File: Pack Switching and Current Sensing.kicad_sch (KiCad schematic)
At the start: 26 parts, among them Q29 CSD19531Q5A, Q30 CSD19531Q5A, Q31 ZXMP10A13F, Q32 CSD19531Q5A, Q33 CSD19531Q5A

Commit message: worked on MCU
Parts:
- renumbered C60 to C24, C62 to C25, C63 to C26, C64 to C27, D79 to D27, D80 to D28, E2 to E1, FB5 to FB1, FB6 to FB2, FB7 to FB3, FB8 to FB4, NT2 to NT1, Q29 to Q11, Q30 to Q12, Q31 to Q13, Q32 to Q14, Q33 to Q15, R153 to R62, R154 to R63, R157 to R64, R158 to R65, R159 to R66, R160 to R67, R163 to R68, R265 to R69, R165 to R70
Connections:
- net SCREW_BATT+ renamed BATT+

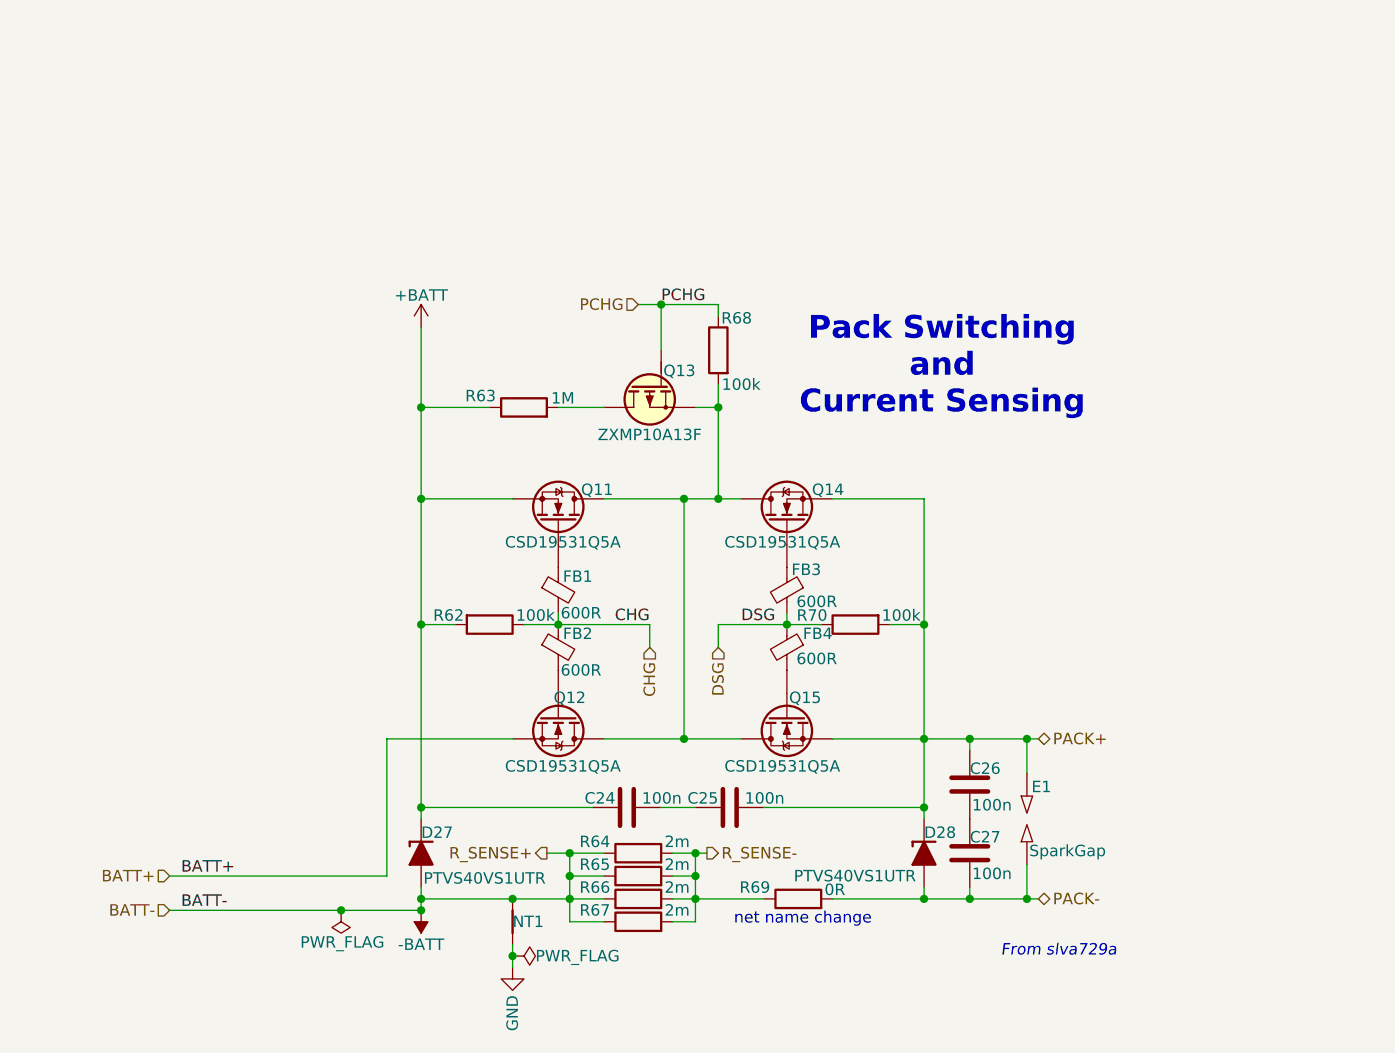
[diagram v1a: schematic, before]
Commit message: Added Fuel/Gas Guage
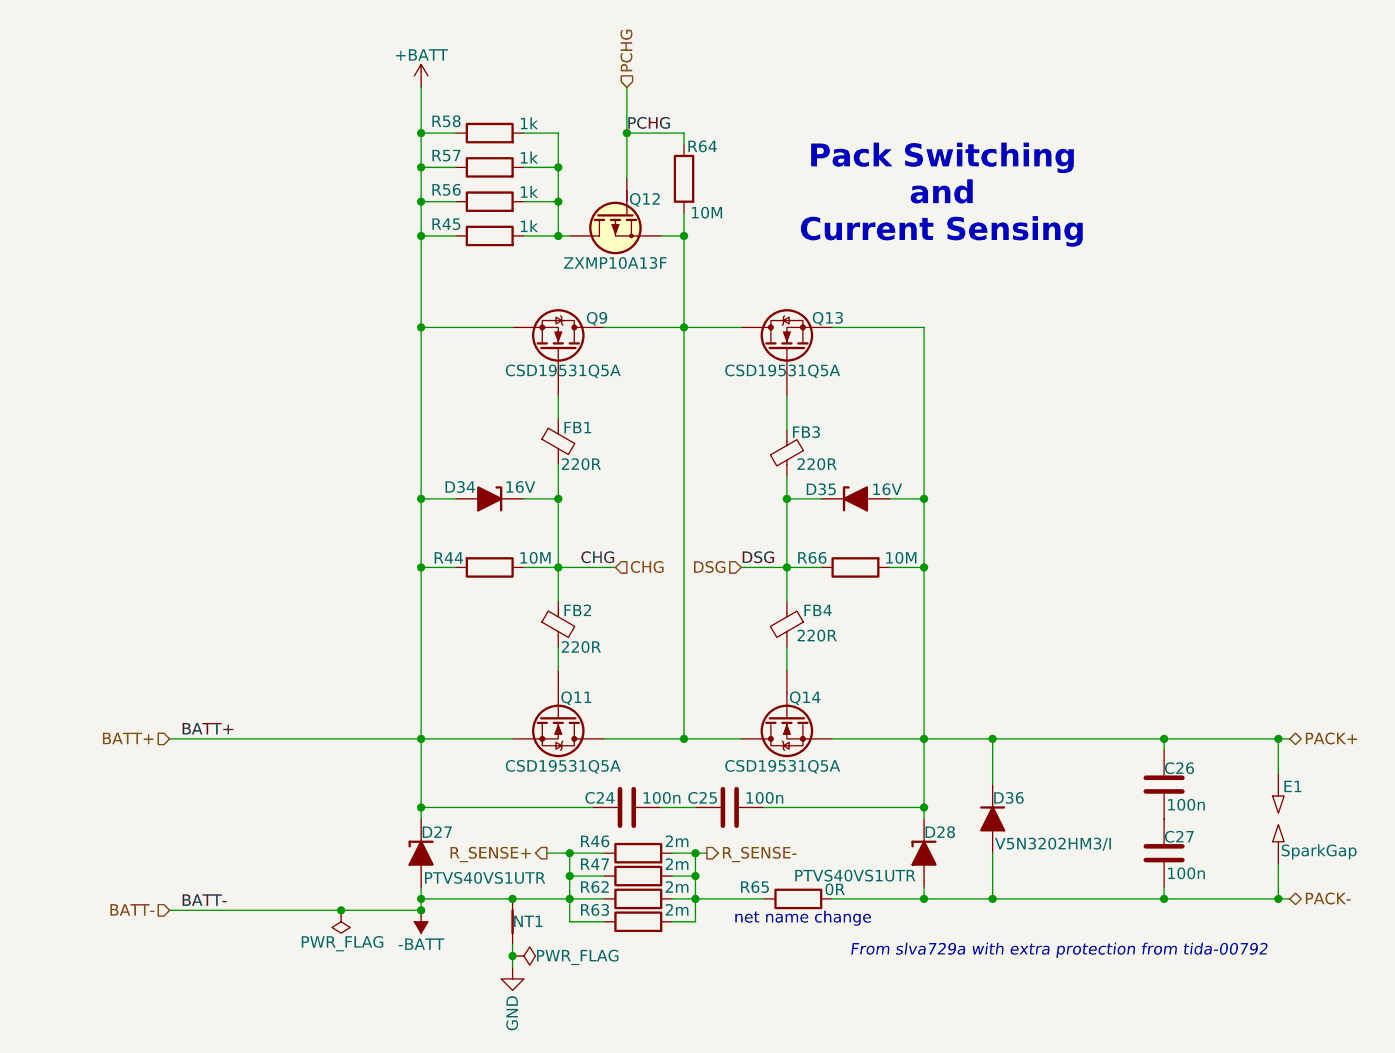
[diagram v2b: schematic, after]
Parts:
- added D34, D35: 16V, symbol Device:D_Zener_Filled
- added D36: V5N3202HM3/I, symbol Device:D_Filled
- added R56, R57, R58: 1k, symbol Device:R
- FB1, FB2, FB3, FB4: value 600R -> 220R
- R44: renamed from R62; value 100k -> 10M
- R45: renamed from R63; value 1M -> 1k
- R64: renamed from R68; value 100k -> 10M
- R66: renamed from R70; value 100k -> 10M
- renumbered Q12 to Q11, Q13 to Q12, Q14 to Q13, Q15 to Q14, Q11 to Q9, R64 to R46, R65 to R47, R66 to R62, R67 to R63, R69 to R65
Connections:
- net BATT+ is gone; now on net +BATT: Q11.1 (S), Q11.2 (S), Q11.3 (S)
- net +BATT: now also D34.2 (A), R56.1, R57.1, R58.1
- net CHG: now also D34.1 (K)
- net DSG: now also D35.1 (K)
- net PACK+: now also D35.2 (A), D36.1 (K)
- net PACK-: now also D36.2 (A)
- net at Q12.3 (D), R45.2: now also R56.2, R57.2, R58.2
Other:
- note added: "From slva729a with extra protection from tida-00792"
- note removed: "From slva729a"
- moved on the sheet: C26, C27, E1, FB1, FB2, FB3, FB4, Q12, Q13, Q9, R44, R45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

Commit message: ready to start first pass review on bms
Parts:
- removed R65: 0R, symbol Device:R
- D24: renamed from D34; value 16V -> 18V
- D25: renamed from D35; value 16V -> 18V
- renumbered C24 to C19, C25 to C20, C26 to C21, C27 to C22, D27 to D23, D28 to D26, D36 to D27, Q11 to Q10, Q12 to Q11, Q13 to Q12, Q14 to Q13, R58 to R44, R57 to R45, R56 to R46, R45 to R47, R44 to R48, R46 to R49, R47 to R50, R62 to R51, R63 to R52, R64 to R53, R66 to R54
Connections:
- net R_SENSE- is gone; now on net PACK-: R49.2, R50.2, R51.2, R52.2
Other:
- note removed: "net name change"

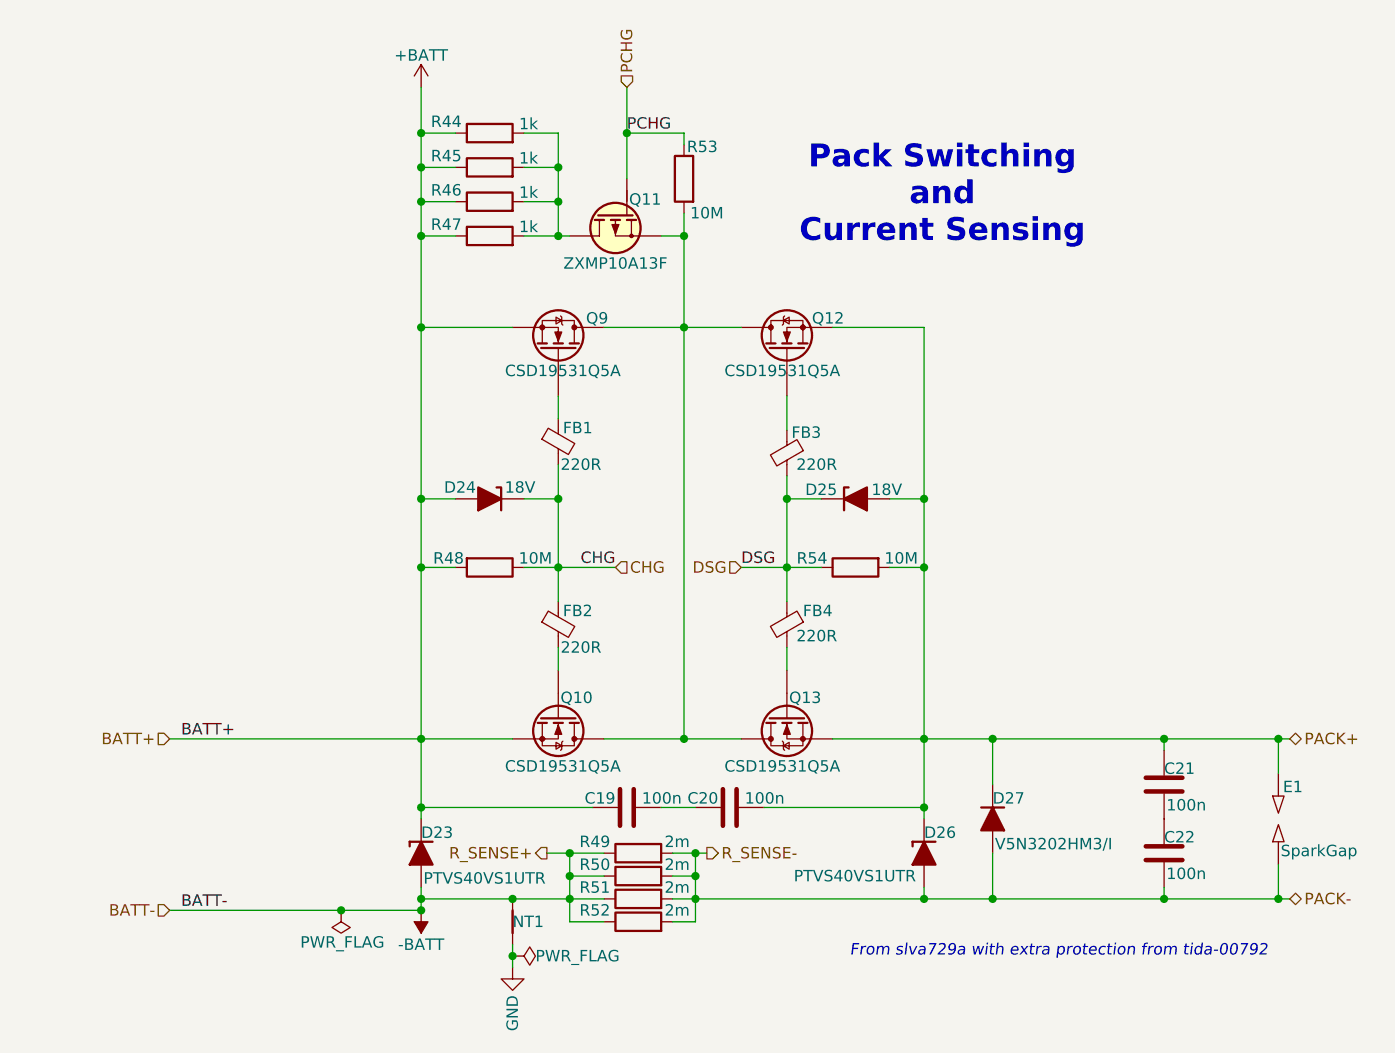
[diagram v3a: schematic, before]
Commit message: I still need to add the 6V line and test points
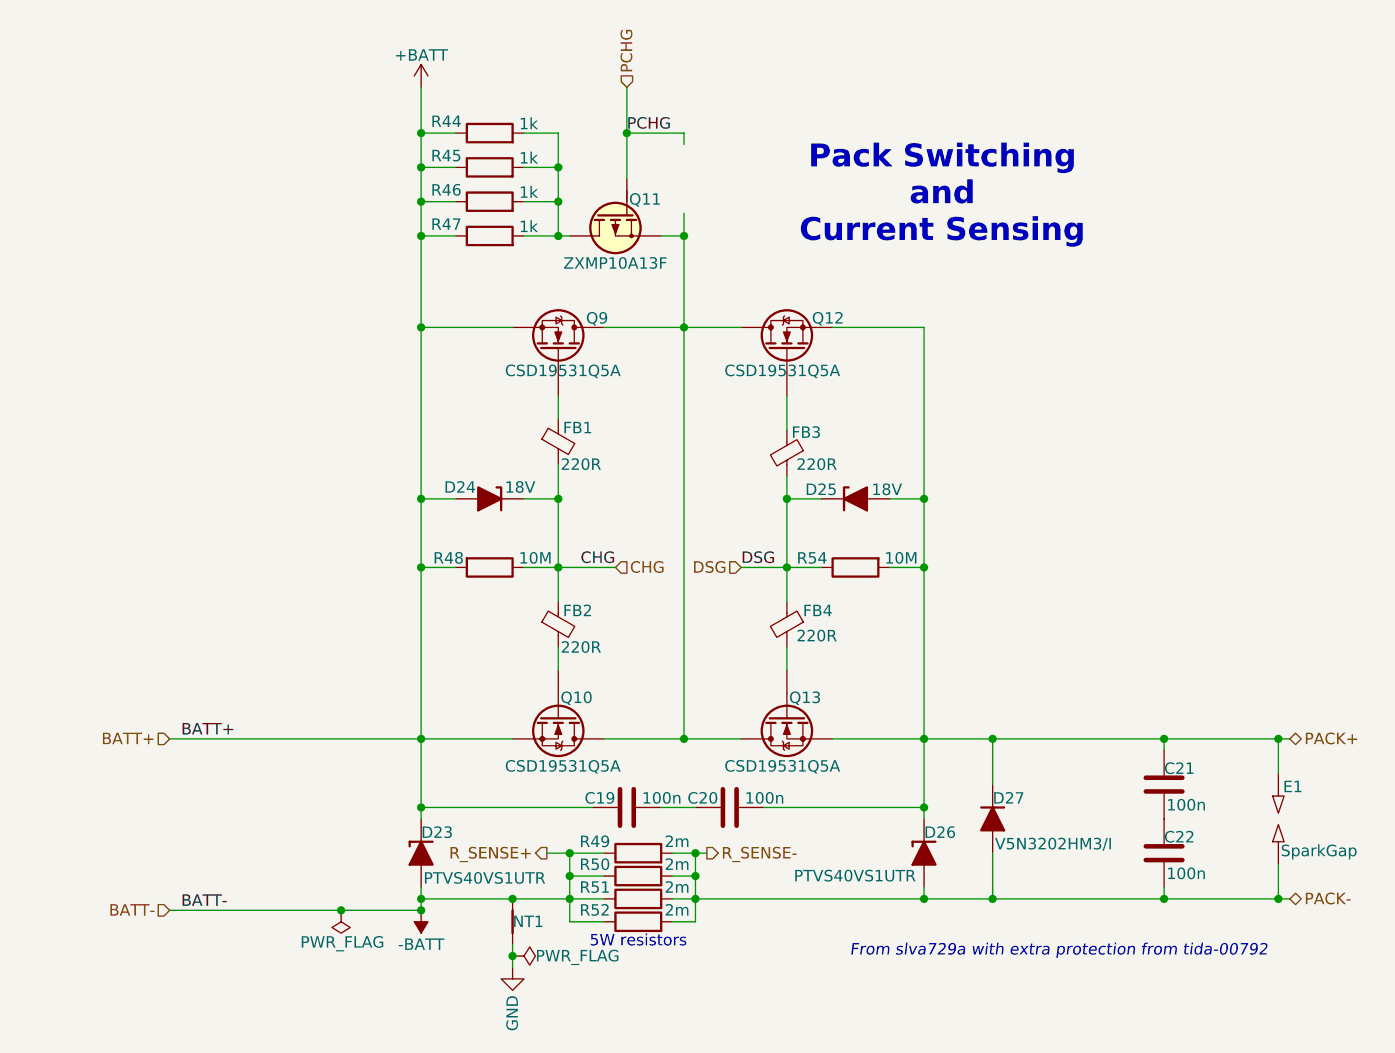
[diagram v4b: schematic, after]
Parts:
- removed R53: 10M, symbol Device:R
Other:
- note added: "5W resistors"
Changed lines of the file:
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@@
 		)
 	)
+	(text "5W resistors"
+		(exclude_from_sim no)
+		(at 140.97 125.476 0)
+		(effects
+			(font
+				(size 1.27 1.27)
+			)
+		)
+	)
 	(junction
 		(at 132.08 43.18)
@@
 					(unit 1)
 				)
-			)
-		)
-	)
-	(symbol
-		(lib_id "Device:R")
-		(at 146.05 40.64 0)
-		(mirror y)
-		(unit 1)
-		(exclude_from_sim no)
-		(in_bom yes)
-		(on_board yes)
-		(dnp no)
-		(property "Reference" "R53"
-			(at 148.082 37.084 0)
-			(effects
-				(font
-					(size 1.27 1.27)
-				)
-			)
-		)
-		(property "Value" "10M"
-			(at 148.59 44.45 0)
-			(effects
-				(font
-					(size 1.27 1.27)
-				)
-			)
-		)
-		(property "Footprint" ""
-			(at 147.828 40.64 90)
-			(effects
-				(font
-					(size 1.27 1.27)
-				)
-				(hide yes)
-			)
-		)
-		(property "Datasheet" "~"
-			(at 146.05 40.64 0)
-			(effects
-				(font
-					(size 1.27 1.27)
-				)
-				(hide yes)
-			)
-		)
-		(property "Description" "Resistor"
-			(at 146.05 40.64 0)
-			(effects
-				(font
-					(size 1.27 1.27)
-				)
-				(hide yes)
-			)
-		)
-		(property "Display" ""
-			(at 146.05 40.64 0)
-			(effects
-				(font
-					(size 1.27 1.27)
-				)
-				(hide yes)
-			)
-		)
-		(property "JLCPCB ID" ""
-			(at 146.05 40.64 0)
-			(effects
-				(font
-					(size 1.27 1.27)
-				)
-				(hide yes)
-			)
-		)
-		(property "LCSC Part" ""
-			(at 146.05 40.64 0)
-			(effects
-				(font
-					(size 1.27 1.27)
-				)
-				(hide yes)
-			)
-		)
-		(pin "1"
-		)
-		(pin "2"
-		)
-		(instances
-			(project "Project-Star"
-				(path "/fc8533bc-25dd-4c20-9b4c-ffebebd6739b/e8da5d81-614b-4fe5-84b3-4c351fab7114/cc0a7e05-dd91-401b-a994-41ee02720f37"
-					(reference "R53")
-					(unit 1)
-				)
